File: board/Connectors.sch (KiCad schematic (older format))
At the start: 3 parts, among them J1 POWER IN, J2 LEFT, J3 RIGHT

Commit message: Added some farnell refs.
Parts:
- J1: Farnell (none) -> 1725656; Ref (none) -> 3041359
- J2, J3: Farnell (none) -> 2779587; Ref (none) -> SSW-115-01-T-S
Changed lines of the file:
@@
 F 2 "Connector_PinSocket_2.54mm:PinSocket_1x15_P2.54mm_Vertical" H 3350 2300 50  0001 C CNN
 F 3 "~" H 3350 2300 50  0001 C CNN
+F 4 "2779587" H 3350 2300 50  0001 C CNN "Farnell"
+F 5 "SSW-115-01-T-S" H 3350 2300 50  0001 C CNN "Ref"
 	1    3350 2300
 	1    0    0    -1
@@
 F 2 "Connector_PinSocket_2.54mm:PinSocket_1x15_P2.54mm_Vertical" H 5150 2300 50  0001 C CNN
 F 3 "~" H 5150 2300 50  0001 C CNN
+F 4 "2779587" H 5150 2300 50  0001 C CNN "Farnell"
+F 5 "SSW-115-01-T-S" H 5150 2300 50  0001 C CNN "Ref"
 	1    5150 2300
 	1    0    0    -1
@@
 F 2 "w_conn_mpt:mpt_0,5-2-2,54" H 2300 5750 50  0001 C CNN
 F 3 "~" H 2300 5750 50  0001 C CNN
+F 4 "1725656" H 2300 5750 50  0001 C CNN "Farnell"
+F 5 "3041359" H 2300 5750 50  0001 C CNN "Ref"
 	1    2300 5750
 	-1   0    0    1

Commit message: Updated some refs.
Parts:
- J1: Farnell 1725656 -> 3041359; Ref 3041359 -> 1725656
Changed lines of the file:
@@
 F 2 "w_conn_mpt:mpt_0,5-2-2,54" H 2300 5750 50  0001 C CNN
 F 3 "~" H 2300 5750 50  0001 C CNN
-F 4 "1725656" H 2300 5750 50  0001 C CNN "Farnell"
-F 5 "3041359" H 2300 5750 50  0001 C CNN "Ref"
+F 4 "3041359" H 2300 5750 50  0001 C CNN "Farnell"
+F 5 "1725656" H 2300 5750 50  0001 C CNN "Ref"
 	1    2300 5750
 	-1   0    0    1

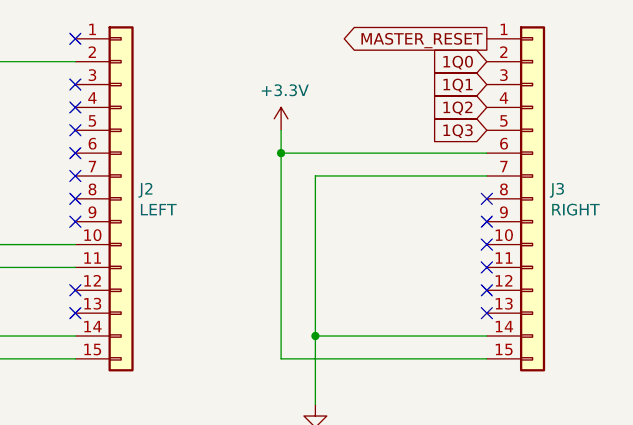
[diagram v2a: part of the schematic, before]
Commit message: /!\ Moved some GPIO (D0,D3 and D4 seem to not be real GPIOs...)
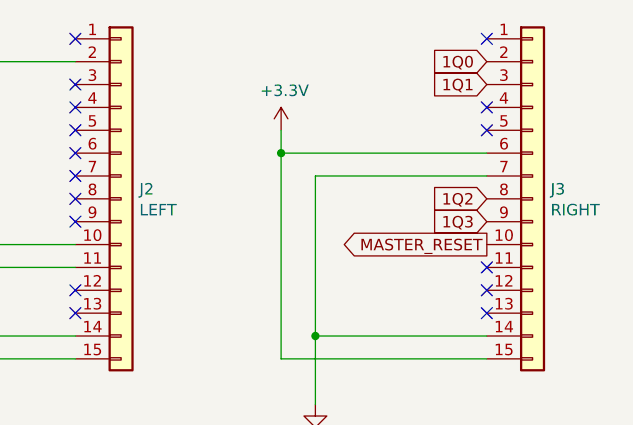
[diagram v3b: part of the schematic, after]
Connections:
- net 1Q2: now also J3.8 (Pin_8); no longer J3.4 (Pin_4)
- net 1Q3: now also J3.9 (Pin_9); no longer J3.5 (Pin_5)
- net MASTER_RESET: now also J3.10 (Pin_10); no longer J3.1 (Pin_1)
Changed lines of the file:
@@
 EESchema Schematic File Version 4
 LIBS:power_stalker_esp-cache
-EELAYER 26 0
+EELAYER 29 0
 EELAYER END
 $Descr A4 11693 8268
@@
 Wire Wire Line
 	2700 5650 3050 5650
-Text GLabel 4950 1600 0    50   Output ~ 0
+Text GLabel 4950 2500 0    50   Output ~ 0
 MASTER_RESET
 Text GLabel 4950 1700 0    50   Input ~ 0
@@
 Text GLabel 4950 1800 0    50   Input ~ 0
 1Q1
-Text GLabel 4950 1900 0    50   Input ~ 0
+Text GLabel 4950 2300 0    50   Input ~ 0
 1Q2
-Text GLabel 4950 2000 0    50   Input ~ 0
+Text GLabel 4950 2400 0    50   Input ~ 0
 1Q3
 NoConn ~ 3150 1600
@@
 NoConn ~ 3150 2700
 NoConn ~ 3150 2800
-NoConn ~ 4950 2300
-NoConn ~ 4950 2400
-NoConn ~ 4950 2500
 NoConn ~ 4950 2600
 NoConn ~ 4950 2700
@@
 Wire Wire Line
 	2050 2600 1750 2600
+NoConn ~ 4950 2000
+NoConn ~ 4950 1900
+NoConn ~ 4950 1600
 $EndSCHEMATC

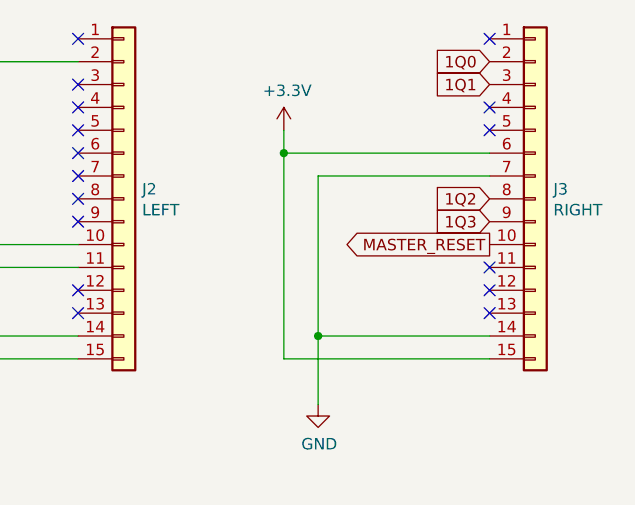
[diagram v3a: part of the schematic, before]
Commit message: Reworked input circuit.
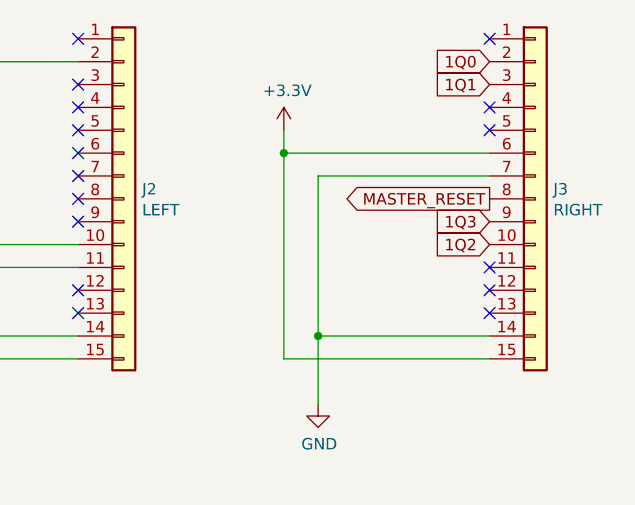
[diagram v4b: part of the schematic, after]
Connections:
- net 1Q2: now also J3.10 (Pin_10); no longer J3.8 (Pin_8)
- net MASTER_RESET: now also J3.8 (Pin_8); no longer J3.10 (Pin_10)
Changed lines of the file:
@@
 Wire Wire Line
 	2700 5650 3050 5650
-Text GLabel 4950 2500 0    50   Output ~ 0
+Text GLabel 4950 2300 0    50   Output ~ 0
 MASTER_RESET
 Text GLabel 4950 1700 0    50   Input ~ 0
@@
 Text GLabel 4950 1800 0    50   Input ~ 0
 1Q1
-Text GLabel 4950 2300 0    50   Input ~ 0
+Text GLabel 4950 2500 0    50   Input ~ 0
 1Q2
 Text GLabel 4950 2400 0    50   Input ~ 0

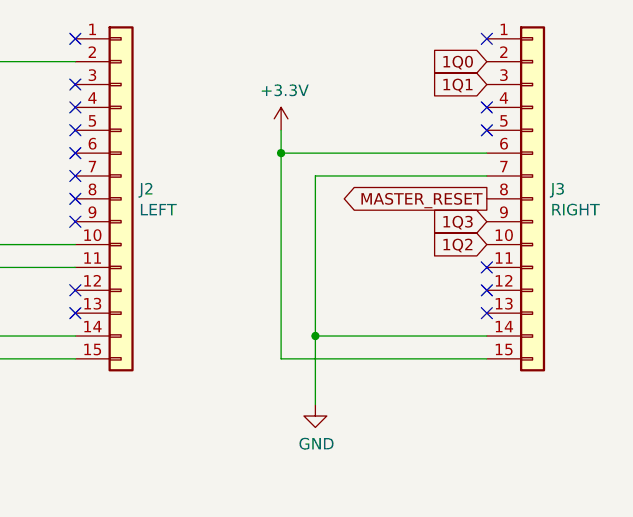
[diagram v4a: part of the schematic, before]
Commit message: Reworked input circuit (again). Added binary counter bypass.
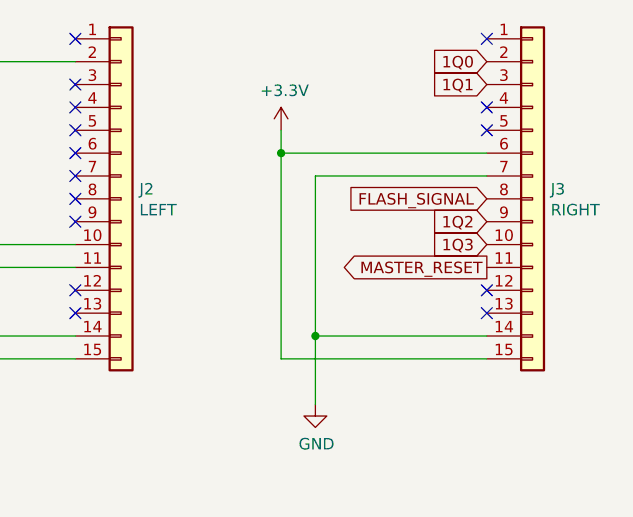
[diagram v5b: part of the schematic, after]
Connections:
- net 1Q2: now also J3.9 (Pin_9); no longer J3.10 (Pin_10)
- net 1Q3: now also J3.10 (Pin_10); no longer J3.9 (Pin_9)
- net MASTER_RESET: now also J3.11 (Pin_11); no longer J3.8 (Pin_8)
- new net FLASH_SIGNAL: J3.8 (Pin_8)
- no-connect marks 16 -> 15
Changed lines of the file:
@@
 EESchema Schematic File Version 4
 LIBS:power_stalker_esp-cache
-EELAYER 29 0
+EELAYER 30 0
 EELAYER END
 $Descr A4 11693 8268
@@
 Wire Wire Line
 	2700 5650 3050 5650
-Text GLabel 4950 2300 0    50   Output ~ 0
+Text GLabel 4950 2600 0    50   Output ~ 0
 MASTER_RESET
 Text GLabel 4950 1700 0    50   Input ~ 0
@@
 Text GLabel 4950 1800 0    50   Input ~ 0
 1Q1
+Text GLabel 4950 2400 0    50   Input ~ 0
+1Q2
 Text GLabel 4950 2500 0    50   Input ~ 0
-1Q2
-Text GLabel 4950 2400 0    50   Input ~ 0
 1Q3
 NoConn ~ 3150 1600
@@
 NoConn ~ 3150 2700
 NoConn ~ 3150 2800
-NoConn ~ 4950 2600
 NoConn ~ 4950 2700
 NoConn ~ 4950 2800
@@
 NoConn ~ 4950 1900
 NoConn ~ 4950 1600
+Text GLabel 4950 2300 0    50   Input ~ 0
+FLASH_SIGNAL
 $EndSCHEMATC
